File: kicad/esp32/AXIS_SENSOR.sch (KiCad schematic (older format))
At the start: 3 parts, among them U10 MPU6500

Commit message: 自動配線成功
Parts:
- renumbered C31 to C26, C32 to C27
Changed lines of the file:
@@
 $Descr A4 11693 8268
 encoding utf-8
-Sheet 8 13
+Sheet 8 14
 Title ""
 Date ""
@@
 	5700 2700 5700 3200
 $Comp
-L GND #PWR047
+L GND #PWR044
 U 1 1 57CCAAFB
 P 5500 4700
-F 0 "#PWR047" H 5500 4450 50  0001 C CNN
+F 0 "#PWR044" H 5500 4450 50  0001 C CNN
 F 1 "GND" H 5500 4550 50  0000 C CNN
 F 2 "" H 5500 4700 50  0000 C CNN
@@
 AXIS_MISO
 $Comp
-L GND #PWR048
+L GND #PWR045
 U 1 1 57CCAB79
 P 6400 4700
-F 0 "#PWR048" H 6400 4450 50  0001 C CNN
+F 0 "#PWR045" H 6400 4450 50  0001 C CNN
 F 1 "GND" H 6400 4550 50  0000 C CNN
 F 2 "" H 6400 4700 50  0000 C CNN
@@
 	6400 3700 6300 3700
 $Comp
-L C C32
+L C C27
 U 1 1 57CCABB6
 P 7200 3950
-F 0 "C32" H 7225 4050 50  0000 L CNN
+F 0 "C27" H 7225 4050 50  0000 L CNN
 F 1 "0.1u" H 7225 3850 50  0000 L CNN
 F 2 "Capacitors_SMD:C_0201" H 7238 3800 50  0001 C CNN
@@
 	7200 3600 6300 3600
 $Comp
-L GND #PWR049
+L GND #PWR046
 U 1 1 57CCAC2E
 P 7200 4700
-F 0 "#PWR049" H 7200 4450 50  0001 C CNN
+F 0 "#PWR046" H 7200 4450 50  0001 C CNN
 F 1 "GND" H 7200 4550 50  0000 C CNN
 F 2 "" H 7200 4700 50  0000 C CNN
@@
 $EndComp
 $Comp
-L C_Small C31
+L C_Small C26
 U 1 1 57CCB9B9
 P 5900 2900
-F 0 "C31" H 5910 2970 50  0000 L CNN
+F 0 "C26" H 5910 2970 50  0000 L CNN
 F 1 "0.1u" H 5910 2820 50  0000 L CNN
 F 2 "Capacitors_SMD:C_0201" H 5900 2900 50  0001 C CNN
@@
 	5500 2900 5800 2900
 $Comp
-L GND #PWR050
+L GND #PWR047
 U 1 1 57CCBA56
 P 6100 3000
-F 0 "#PWR050" H 6100 2750 50  0001 C CNN
+F 0 "#PWR047" H 6100 2750 50  0001 C CNN
 F 1 "GND" H 6100 2850 50  0000 C CNN
 F 2 "" H 6100 3000 50  0000 C CNN
@@
 AXIS_CAP
 $Comp
-L +3.3V #PWR051
+L +3.3V #PWR048
 U 1 1 589CBD39
 P 5700 2700
-F 0 "#PWR051" H 5700 2550 50  0001 C CNN
+F 0 "#PWR048" H 5700 2550 50  0001 C CNN
 F 1 "+3.3V" H 5700 2840 50  0000 C CNN
 F 2 "" H 5700 2700 50  0000 C CNN

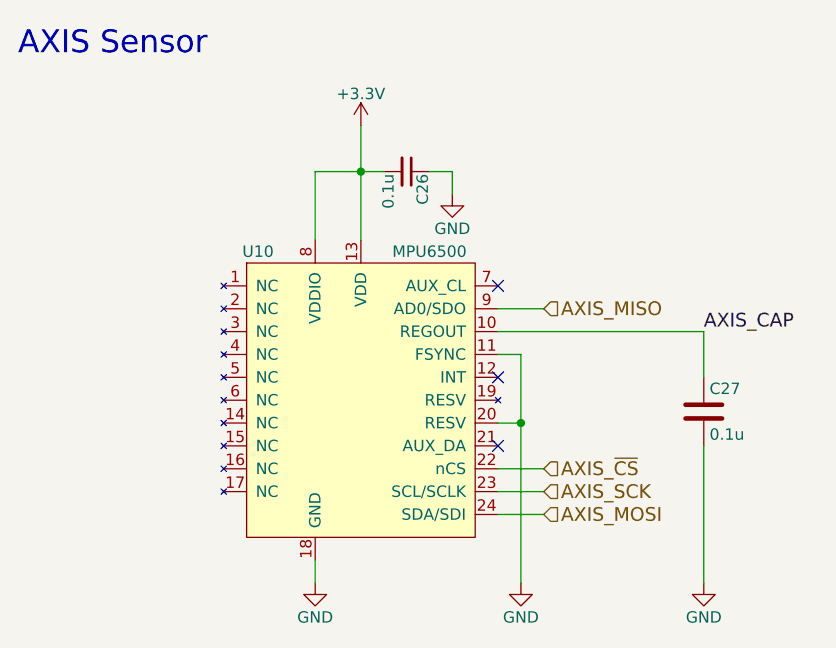
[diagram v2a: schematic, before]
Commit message: 2輪の基板を作成
部品を配置
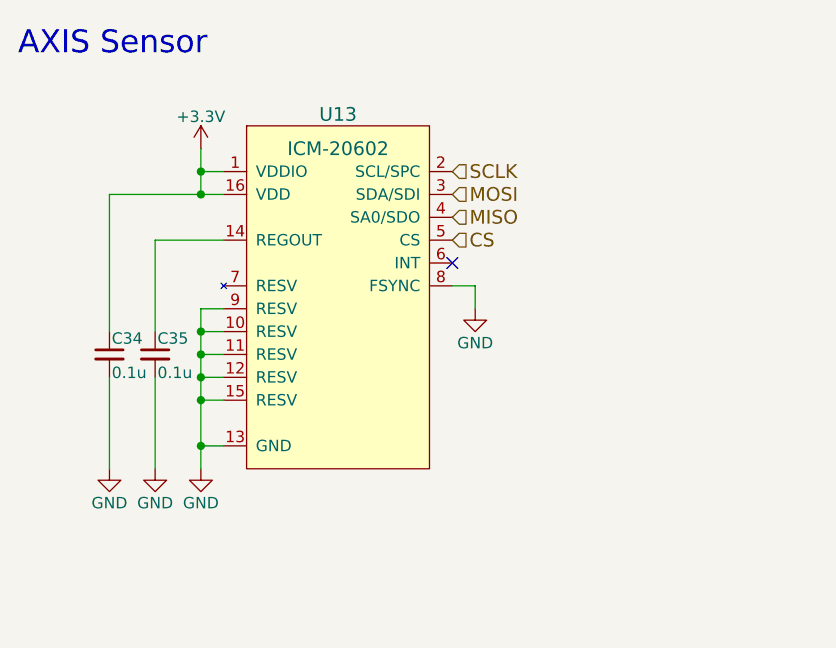
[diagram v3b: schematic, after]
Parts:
- removed C26: 0.1u, Capacitors_SMD:C_0201, symbol C_Small
- removed C27: 0.1u, Capacitors_SMD:C_0201, symbol C
- removed U10: MPU6500, mouse:MPU6500, symbol MPU6500
- added C34, C35: 0.1u, Capacitors_SMD:C_0201, symbol C_Small
- added U13: ICM-20602, mouse:LGA-16-3x3, symbol ICM-20602
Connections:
- net +3V3: now also C34.1, U13.1 (VDDIO), U13.16 (VDD)
- net GND: now also C34.2, C35.2, U13.10 (RESV), U13.11 (RESV), U13.12 (RESV), U13.13 (GND), U13.15 (RESV), U13.8 (FSYNC), U13.9 (RESV)
- new net: C35.1, U13.14 (REGOUT)
- new net CS: U13.5 (CS)
- new net MISO: U13.4 (SA0/SDO)
- new net MOSI: U13.3 (SDA/SDI)
- new net SCLK: U13.2 (SCL/SPC)
- no-connect marks 3 -> 1
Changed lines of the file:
@@
 $Descr A4 11693 8268
 encoding utf-8
-Sheet 8 14
+Sheet 13 13
 Title ""
 Date ""
@@
 Comment4 ""
 $EndDescr
-Wire Wire Line
-	5700 2700 5700 3200
+Text Notes 4200 2400 0    100  ~ 0
+AXIS Sensor
 $Comp
-L GND #PWR044
-U 1 1 57CCAAFB
-P 5500 4700
-F 0 "#PWR044" H 5500 4450 50  0001 C CNN
-F 1 "GND" H 5500 4550 50  0000 C CNN
-F 2 "" H 5500 4700 50  0000 C CNN
-F 3 "" H 5500 4700 50  0000 C CNN
-	1    5500 4700
+L ICM-20602 U13
+U 1 1 592C611A
+P 5600 3400
+F 0 "U13" H 5600 4150 60  0000 C CNN
+F 1 "ICM-20602" H 5600 4000 60  0000 C CNN
+F 2 "mouse:LGA-16-3x3" H 5600 4000 60  0001 C CNN
+F 3 "" H 5600 4000 60  0000 C CNN
+	1    5600 3400
+	1    0    0    -1
+$EndComp
+$Comp
+L C_Small C35
+U 1 1 592C613A
+P 4800 3700
+F 0 "C35" H 4810 3770 50  0000 L CNN
+F 1 "0.1u" H 4810 3620 50  0000 L CNN
+F 2 "Capacitors_SMD:C_0201" H 4800 3700 50  0001 C CNN
+F 3 "" H 4800 3700 50  0000 C CNN
+	1    4800 3700
+	1    0    0    -1
+$EndComp
+$Comp
+L C_Small C34
+U 1 1 592C6186
+P 4600 3700
+F 0 "C34" H 4610 3770 50  0000 L CNN
+F 1 "0.1u" H 4610 3620 50  0000 L CNN
+F 2 "Capacitors_SMD:C_0201" H 4600 3700 50  0001 C CNN
+F 3 "" H 4600 3700 50  0000 C CNN
+	1    4600 3700
+	1    0    0    -1
+$EndComp
+$Comp
+L GND #PWR068
+U 1 1 592C63E1
+P 5000 4200
+F 0 "#PWR068" H 5000 3950 50  0001 C CNN
+F 1 "GND" H 5000 4050 50  0000 C CNN
+F 2 "" H 5000 4200 50  0000 C CNN
+F 3 "" H 5000 4200 50  0000 C CNN
+	1    5000 4200
+	1    0    0    -1
+$EndComp
+$Comp
+L GND #PWR069
+U 1 1 592C640D
+P 4800 4200
+F 0 "#PWR069" H 4800 3950 50  0001 C CNN
+F 1 "GND" H 4800 4050 50  0000 C CNN
+F 2 "" H 4800 4200 50  0000 C CNN
+F 3 "" H 4800 4200 50  0000 C CNN
+	1    4800 4200
+	1    0    0    -1
+$EndComp
+$Comp
+L GND #PWR070
+U 1 1 592C6444
+P 4600 4200
+F 0 "#PWR070" H 4600 3950 50  0001 C CNN
+F 1 "GND" H 4600 4050 50  0000 C CNN
+F 2 "" H 4600 4200 50  0000 C CNN
+F 3 "" H 4600 4200 50  0000 C CNN
+	1    4600 4200
+	1    0    0    -1
+$EndComp
+$Comp
+L +3.3V #PWR071
+U 1 1 592C64FB
+P 5000 2800
+F 0 "#PWR071" H 5000 2650 50  0001 C CNN
+F 1 "+3.3V" H 5000 2940 50  0000 C CNN
+F 2 "" H 5000 2800 50  0000 C CNN
+F 3 "" H 5000 2800 50  0000 C CNN
+	1    5000 2800
+	1    0    0    -1
+$EndComp
+Text HLabel 6100 3100 2    60   Input ~ 0
+MISO
+NoConn ~ 6100 3300
+$Comp
+L GND #PWR072
+U 1 1 592C6B85
+P 6200 3500
+F 0 "#PWR072" H 6200 3250 50  0001 C CNN
+F 1 "GND" H 6200 3350 50  0000 C CNN
+F 2 "" H 6200 3500 50  0000 C CNN
+F 3 "" H 6200 3500 50  0000 C CNN
+	1    6200 3500
 	1    0    0    -1
 $EndComp
 Wire Wire Line
-	5500 4700 5500 4600
-NoConn ~ 6300 3400
-NoConn ~ 6300 4100
-Text HLabel 6500 4200 2    60   Input ~ 0
-AXIS_~CS
-Text HLabel 6500 4300 2    60   Input ~ 0
-AXIS_SCK
-Text HLabel 6500 4400 2    60   Input ~ 0
-AXIS_MOSI
-Text HLabel 6500 3500 2    60   Input ~ 0
-AXIS_MISO
-$Comp
-L GND #PWR045
-U 1 1 57CCAB79
-P 6400 4700
-F 0 "#PWR045" H 6400 4450 50  0001 C CNN
-F 1 "GND" H 6400 4550 50  0000 C CNN
-F 2 "" H 6400 4700 50  0000 C CNN
-F 3 "" H 6400 4700 50  0000 C CNN
-	1    6400 4700
-	1    0    0    -1
-$EndComp
+	4600 3000 5100 3000
+Connection ~ 5000 2900
 Wire Wire Line
-	6400 4700 6400 3700
+	5000 2900 5100 2900
+Connection ~ 5000 3000
 Wire Wire Line
-	6400 3700 6300 3700
-$Comp
-L C C27
-U 1 1 57CCABB6
-P 7200 3950
-F 0 "C27" H 7225 4050 50  0000 L CNN
-F 1 "0.1u" H 7225 3850 50  0000 L CNN
-F 2 "Capacitors_SMD:C_0201" H 7238 3800 50  0001 C CNN
-F 3 "" H 7200 3950 50  0000 C CNN
-	1    7200 3950
-	1    0    0    -1
-$EndComp
+	5000 2800 5000 3000
 Wire Wire Line
-	7200 3800 7200 3600
+	4600 4200 4600 3800
 Wire Wire Line
-	7200 3600 6300 3600
-$Comp
-L GND #PWR046
-U 1 1 57CCAC2E
-P 7200 4700
-F 0 "#PWR046" H 7200 4450 50  0001 C CNN
-F 1 "GND" H 7200 4550 50  0000 C CNN
-F 2 "" H 7200 4700 50  0000 C CNN
-F 3 "" H 7200 4700 50  0000 C CNN
-	1    7200 4700
-	1    0    0    -1
-$EndComp
+	4800 3200 5100 3200
 Wire Wire Line
-	7200 4700 7200 4100
+	4800 3600 4800 3200
 Wire Wire Line
-	6300 4000 6400 4000
-Connection ~ 6400 4000
+	4800 4200 4800 3800
+Connection ~ 5000 4100
+Connection ~ 5000 3600
 Wire Wire Line
-	6500 3500 6300 3500
+	5000 3500 5100 3500
+Connection ~ 5000 3700
 Wire Wire Line
-	6500 4200 6300 4200
+	5000 3600 5100 3600
+Connection ~ 5000 3800
 Wire Wire Line
-	6300 4300 6500 4300
+	5000 3700 5100 3700
+Connection ~ 5000 3900
 Wire Wire Line
-	6500 4400 6300 4400
-$Comp
-L MPU6500 U10
-U 1 1 57CCB62A
-P 5700 3650
-F 0 "U10" H 5250 4050 50  0000 C CNN
-F 1 "MPU6500" H 6000 4050 50  0000 C CNN
-F 2 "mouse:MPU6500" H 5100 2650 50  0001 C CNN
-F 3 "DOCUMENTATION" H 5250 2550 50  0001 C CNN
-	1    5700 3650
-	1    0    0    -1
-$EndComp
-$Comp
-L C_Small C26
-U 1 1 57CCB9B9
-P 5900 2900
-F 0 "C26" H 5910 2970 50  0000 L CNN
-F 1 "0.1u" H 5910 2820 50  0000 L CNN
-F 2 "Capacitors_SMD:C_0201" H 5900 2900 50  0001 C CNN
-F 3 "" H 5900 2900 50  0000 C CNN
-	1    5900 2900
-	0    1    1    0
-$EndComp
-Connection ~ 5700 2900
+	5100 3800 5000 3800
 Wire Wire Line
-	5500 2900 5800 2900
-$Comp
-L GND #PWR047
-U 1 1 57CCBA56
-P 6100 3000
-F 0 "#PWR047" H 6100 2750 50  0001 C CNN
-F 1 "GND" H 6100 2850 50  0000 C CNN
-F 2 "" H 6100 3000 50  0000 C CNN
-F 3 "" H 6100 3000 50  0000 C CNN
-	1    6100 3000
-	1    0    0    -1
-$EndComp
+	5000 3900 5100 3900
 Wire Wire Line
-	6100 3000 6100 2900
+	5000 3500 5000 4200
 Wire Wire Line
-	6100 2900 6000 2900
-Text Notes 4200 2400 0    100  ~ 0
-AXIS Sensor
-Text Label 7200 3600 0    60   ~ 0
-AXIS_CAP
-$Comp
-L +3.3V #PWR048
-U 1 1 589CBD39
-P 5700 2700
-F 0 "#PWR048" H 5700 2550 50  0001 C CNN
-F 1 "+3.3V" H 5700 2840 50  0000 C CNN
-F 2 "" H 5700 2700 50  0000 C CNN
-F 3 "" H 5700 2700 50  0000 C CNN
-	1    5700 2700
-	1    0    0    -1
-$EndComp
+	5000 4100 5100 4100
 Wire Wire Line
-	5500 3200 5500 2900
-NoConn ~ 6300 3800
+	4600 3000 4600 3600
+Wire Wire Line
+	6100 3400 6200 3400
+Wire Wire Line
+	6200 3400 6200 3500
+Text HLabel 6100 3000 2    60   Input ~ 0
+MOSI
+Text HLabel 6100 3200 2    60   Input ~ 0
+CS
+Text HLabel 6100 2900 2    60   Input ~ 0
+SCLK
 $EndSCHEMATC
